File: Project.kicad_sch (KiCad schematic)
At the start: 21 parts, among them P1 USB_C_Plug, SW1 DOUBLE_KEY, U1 MAX15062A, U2 TUSB8041, Y1 24MHz

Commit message: 原理图完工
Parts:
- added C10, C11, C12, C13, C8, C9: 0.1uF, symbol Lib1:C(MM)-LibCool
- added C? (x2): 18pF, symbol Lib1:C(MM)-LibCool
- added C?: 4.7uF, symbol Lib1:C(MM)-LibCool
- added D1: OVERCUR1, symbol Device:LED
- added D2, D3: OVERCUR2, symbol Device:LED
- added J1, J2: USB3_A, symbol Connector:USB3_A
- added J?: RJ45, symbol Connector:RJ45
- added P2: USB_C_Plug, symbol Connector:USB_C_Plug
- added R10, R11: RES(M)-LibCool, symbol Lib1:RES(M)-LibCool
- added R9: 4.7K/5%, symbol Lib1:RES(M)-LibCool
- added R?: 226R/1%, symbol Lib1:RES(M)-LibCool
- added U?: XR22800, symbol Lib1:XR22800
- added Y?: 25MHz, symbol Lib1:OSC-LibCool
- gave numbers to parts that had none: 4
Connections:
- net +3V3: now also U2.16 (VDD33), U2.26 (USB_SSTXP_DN4), U2.34 (VDD33), U2.52 (VDD33), U2.63 (VDD33), C13.1, R10.1, R11.1, R9.1, U?.1 (VBUS_SENSE)
- net GND: now also U2.65 (VSS), C?.2, C?.2, C?.2, D1.1 (K), D2.1 (K), D3.1 (K), R?.2, U?.12 (GND), U?.21 (GND), U?.22 (GND), U?.28 (GND), U?.4 (GND)
- net POWER: now also J1.1 (VBUS), U?.7 (VCC)
- net at U2.1 (USB_DP_DN1): now also J1.3 (D+)
- net ETH_D-: now reaches U2.10 (USB_DM_DN2)
- net ETH_D-: now also U?.5 (USBD-)
- net at U2.17 (USB_DP_DN3): now also J2.3 (D+)
- net at U2.18 (USB_DM_DN3): now also J2.2 (D-)
- net at U2.19 (USB_SSTXP_DN3): now also C8.1
- net at U2.2 (USB_DM_DN1): now also J1.2 (D-)
- net at U2.20 (USB_SSTXM_DN3): now also C10.1
- net at U2.22 (USB_SSRXP_DN3): now also J2.6 (SSRX+)
- net at U2.23 (USB_SSRXM_DN3): now also J2.5 (SSRX-)
- net at U2.24 (USB_DP_DN4): now also P2.A6 (D+)
- net at U2.25 (USB_DM_DN4): now also P2.A7 (D-)
- net at U2.27 (USB_SSTXM_DN4): now also C12.1
- net at U2.29 (USB_SSRXP_DN4): now also P2.B11 (RX1+)
- net at U2.3 (USB_SSTXP_DN1): now also C9.1
- net at U2.30 (USB_SSRXM_DN4): now also P2.B10 (RX1-)
- net at U2.32 (PWRCTL4/BATEN4): now also R11.2
- net at U2.33 (PWRCTL3/BATEN3): now also R10.2
- net at U2.36 (PWRCTL1/BATEN1): now also R9.2
- net at U2.4 (USB_SSTXM_DN1): now also C11.1
- net at U2.43 (OVERCUR4z): now also D3.2 (A)
- net at U2.44 (OVERCUR3z): now also D2.2 (A)
- net at U2.46 (OVERCUR1z): now also D1.2 (A)
- net at U2.6 (USB_SSRXP_DN1): now also J1.6 (SSRX+)
- net at U2.7 (USB_SSRXM_DN1): now also J1.5 (SSRX-)
- net ETH_D+: now reaches U2.9 (USB_DP_DN2)
- net ETH_D+: now also U?.6 (USBD+)
- new net: C13.2, P2.A2 (TX1+)
- new net: C11.2, J1.8 (SSTX-)
- new net: C9.2, J1.9 (SSTX+)
- new net: C?.1, U?.10 (XTALIN), Y?.1
- new net: C?.1, U?.11 (3V3_OUT), U?.20 (CAP2), U?.3 (CAP1)
- new net: J?.2, U?.13 (ETH_TX-)
- new net: J?.1, U?.14 (ETH_TX+)
- new net: J?.3, U?.15 (ETH_RX+)
- new net: J?.6, U?.16 (ETH_RX-)
- new net: R?.1, U?.2 (REXT)
- new net: C?.1, U?.9 (XTALOUT), Y?.2
- new net: C12.2, P2.A3 (TX1-)
- new net: C10.2, J2.8 (SSTX-)
- new net: C8.2, J2.9 (SSTX+)
- new net: P2.A1 (GND), P2.A12 (GND), P2.B1 (GND), P2.B12 (GND)
- new net: P2.A4 (VBUS), P2.A9 (VBUS), P2.B4 (VBUS), P2.B9 (VBUS)
- no-connect marks 0 -> 22

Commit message: 画错了.png
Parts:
- R10, R11: value RES(M)-LibCool -> 4.7K/5%
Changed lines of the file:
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@@
       (effects (font (size 0.9906 0.9906)) (justify right))
     )
-    (property "Value" "RES(M)-LibCool" (id 1) (at 188.087 98.7288 90)
+    (property "Value" "4.7K/5%" (id 1) (at 188.087 98.7288 90)
       (effects (font (size 0.9906 0.9906)) (justify right))
     )
@@
       (effects (font (size 0.9906 0.9906)) (justify right))
     )
-    (property "Value" "RES(M)-LibCool" (id 1) (at 188.087 121.5888 90)
+    (property "Value" "4.7K/5%" (id 1) (at 188.087 121.5888 90)
       (effects (font (size 0.9906 0.9906)) (justify right))
     )
@@
     )
     (path "/89fb6906-a42e-497c-a7b2-25a3431a4030"
-      (reference "R10") (unit 1) (value "RES(M)-LibCool") (footprint "")
+      (reference "R10") (unit 1) (value "4.7K/5%") (footprint "")
     )
     (path "/df5779d8-f968-49f0-8166-ee0ca7a408f9"
-      (reference "R11") (unit 1) (value "RES(M)-LibCool") (footprint "")
+      (reference "R11") (unit 1) (value "4.7K/5%") (footprint "")
     )
     (path "/cb8a80c4-ebc1-408e-9240-fd24926bdfee"

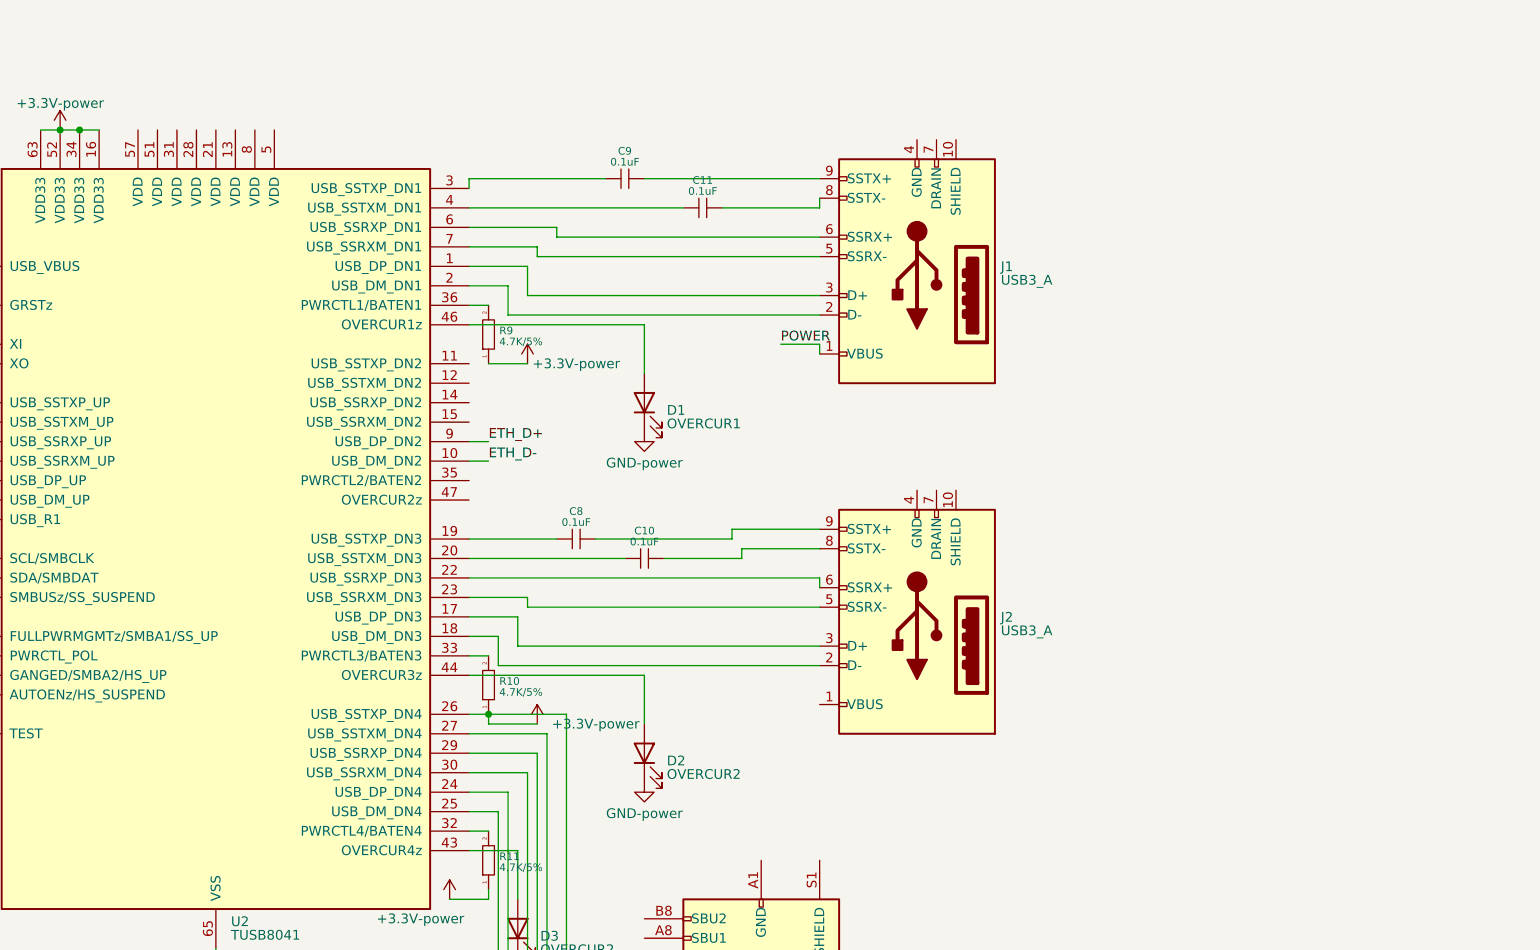
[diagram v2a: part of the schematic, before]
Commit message: 添加1.1v降压部分
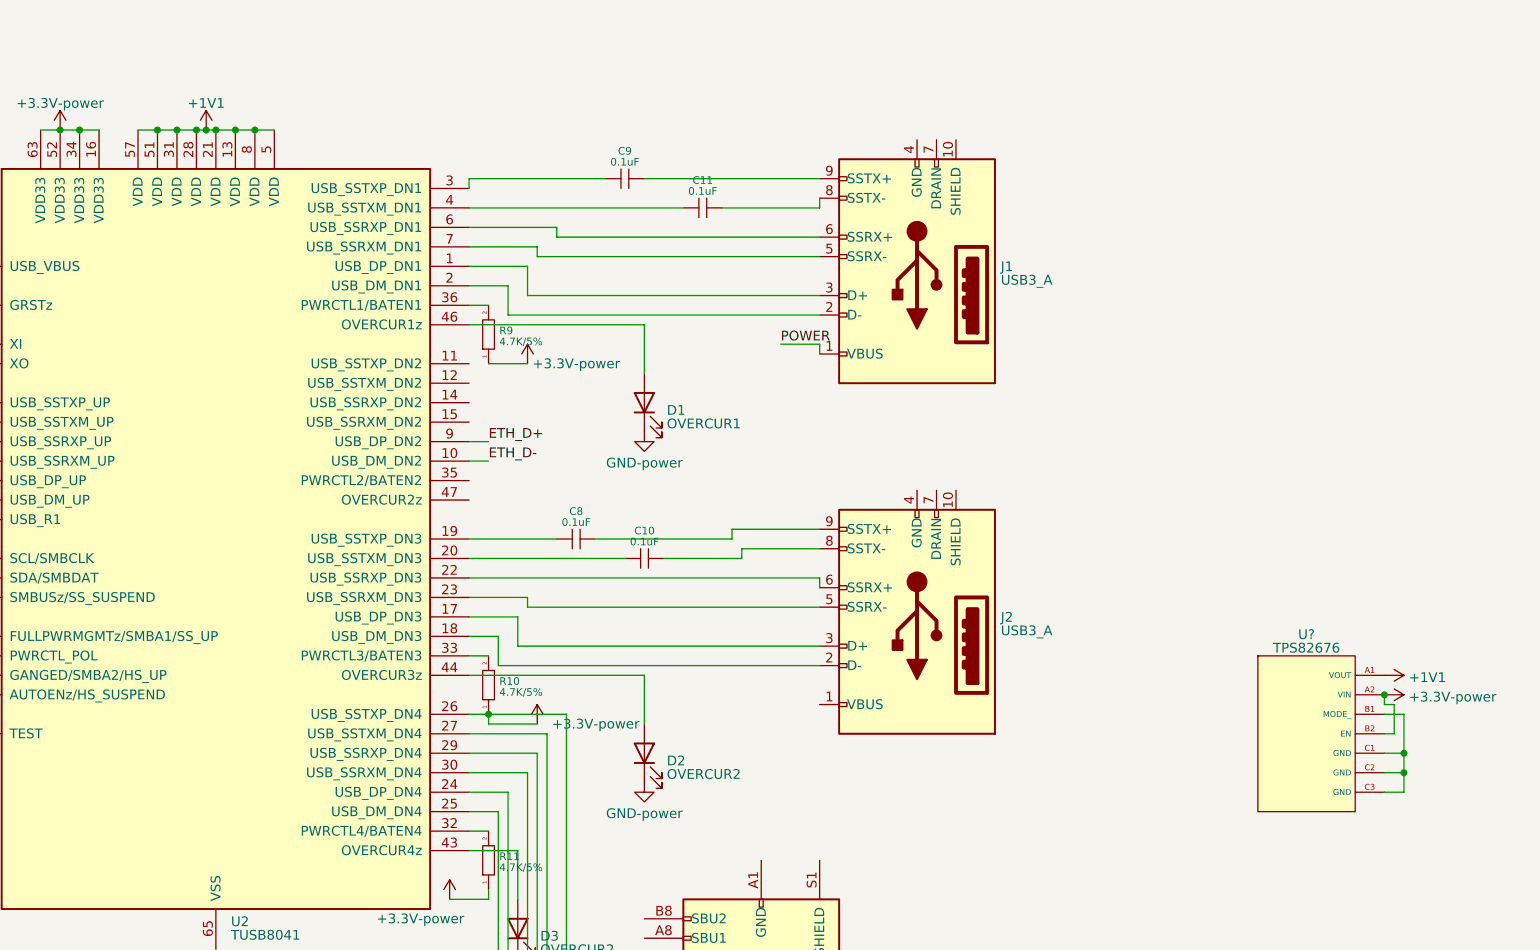
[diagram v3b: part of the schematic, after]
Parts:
- added U?: TPS82676, symbol Lib1:TPS82676
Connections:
- net +3V3: now also U?.A2 (VIN), U?.B2 (EN)
- net +1V1: now reaches U2.13 (VDD)
- net +1V1: now also U2.21 (VDD), U2.28 (VDD), U2.31 (VDD), U2.5 (VDD), U2.51 (VDD), U2.57 (VDD), U2.8 (VDD), U?.A1 (VOUT)
- new net: U?.B1 (MODE_), U?.C1 (GND), U?.C2 (GND), U?.C3 (GND)
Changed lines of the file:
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@@
   (junction (at 64.77 176.53) (diameter 0) (color 0 0 0 0)
   )
+  (junction (at 146.05 25.4) (diameter 0) (color 0 0 0 0)
+  )
   (junction (at 49.53 204.47) (diameter 0) (color 0 0 0 0)
   )
+  (junction (at 303.53 99.06) (diameter 0) (color 0 0 0 0)
+  )
   (junction (at 48.26 204.47) (diameter 0) (color 0 0 0 0)
   )
@@
   (junction (at 60.96 177.8) (diameter 0) (color 0 0 0 0)
   )
+  (junction (at 306.07 109.22) (diameter 0) (color 0 0 0 0)
+  )
   (junction (at 133.35 25.4) (diameter 0) (color 0 0 0 0)
   )
   (junction (at 58.42 194.31) (diameter 0) (color 0 0 0 0)
   )
+  (junction (at 143.51 25.4) (diameter 0) (color 0 0 0 0)
+  )
   (junction (at 69.85 177.8) (diameter 0) (color 0 0 0 0)
   )
+  (junction (at 149.86 25.4) (diameter 0) (color 0 0 0 0)
+  )
   (junction (at 101.6 54.61) (diameter 0) (color 0 0 0 0)
   )
   (junction (at 110.49 43.18) (diameter 0) (color 0 0 0 0)
   )
+  (junction (at 153.67 25.4) (diameter 0) (color 0 0 0 0)
+  )
   (junction (at 130.81 25.4) (diameter 0) (color 0 0 0 0)
   )
@@
   (junction (at 24.13 86.36) (diameter 0) (color 0 0 0 0)
   )
+  (junction (at 156.21 25.4) (diameter 0) (color 0 0 0 0)
+  )
   (junction (at 114.3 50.8) (diameter 0) (color 0 0 0 0)
   )
+  (junction (at 306.07 106.68) (diameter 0) (color 0 0 0 0)
+  )
   (junction (at 106.68 58.42) (diameter 0) (color 0 0 0 0)
   )
@@
   )
   (junction (at 114.3 58.42) (diameter 0) (color 0 0 0 0)
+  )
+  (junction (at 151.13 25.4) (diameter 0) (color 0 0 0 0)
+  )
+  (junction (at 148.59 25.4) (diameter 0) (color 0 0 0 0)
   )
   (no_connect (at 39.37 186.69))
@@
   (no_connect (at 43.18 78.74))
   (no_connect (at 57.15 193.04))
+  (wire (pts (xy 306.07 101.6) (xy 306.07 106.68))
+    (stroke (width 0) (type default))
+  )
+  (wire (pts (xy 143.51 25.4) (xy 146.05 25.4))
+    (stroke (width 0) (type default))
+  )
   (wire (pts (xy 110.49 43.18) (xy 118.11 43.18))
     (stroke (width 0) (type default))
@@
     (stroke (width 0) (type default))
   )
+  (wire (pts (xy 151.13 25.4) (xy 153.67 25.4))
+    (stroke (width 0) (type default))
+  )
   (wire (pts (xy 184.15 50.8) (xy 207.01 50.8))
     (stroke (width 0) (type default))
@@
     (stroke (width 0) (type default))
   )
+  (wire (pts (xy 303.53 109.22) (xy 306.07 109.22))
+    (stroke (width 0) (type default))
+  )
   (wire (pts (xy 193.04 106.68) (xy 193.04 158.75))
     (stroke (width 0) (type default))
@@
     (stroke (width 0) (type default))
   )
+  (wire (pts (xy 153.67 25.4) (xy 156.21 25.4))
+    (stroke (width 0) (type default))
+  )
   (wire (pts (xy 229.87 46.99) (xy 191.77 46.99))
     (stroke (width 0) (type default))
   )
+  (wire (pts (xy 306.07 109.22) (xy 306.07 106.68))
+    (stroke (width 0) (type default))
+  )
   (wire (pts (xy 114.3 63.5) (xy 118.11 63.5))
     (stroke (width 0) (type default))
@@
     (stroke (width 0) (type default))
   )
+  (wire (pts (xy 306.07 109.22) (xy 306.07 111.76))
+    (stroke (width 0) (type default))
+  )
   (wire (pts (xy 189.23 49.53) (xy 229.87 49.53))
     (stroke (width 0) (type default))
@@
     (stroke (width 0) (type default))
   )
+  (wire (pts (xy 156.21 25.4) (xy 158.75 25.4))
+    (stroke (width 0) (type default))
+  )
   (wire (pts (xy 34.29 121.92) (xy 35.56 121.92))
     (stroke (width 0) (type default))
@@
     (stroke (width 0) (type default))
   )
+  (wire (pts (xy 306.07 111.76) (xy 303.53 111.76))
+    (stroke (width 0) (type default))
+  )
   (wire (pts (xy 191.77 161.29) (xy 207.01 161.29))
     (stroke (width 0) (type default))
@@
     (stroke (width 0) (type default))
   )
+  (wire (pts (xy 148.59 25.4) (xy 149.86 25.4))
+    (stroke (width 0) (type default))
+  )
   (wire (pts (xy 207.01 96.52) (xy 207.01 102.87))
     (stroke (width 0) (type default))
@@
     (stroke (width 0) (type default))
   )
+  (wire (pts (xy 304.8 100.33) (xy 304.8 104.14))
+    (stroke (width 0) (type default))
+  )
   (wire (pts (xy 200.66 78.74) (xy 218.44 78.74))
     (stroke (width 0) (type default))
@@
     (stroke (width 0) (type default))
   )
+  (wire (pts (xy 303.53 99.06) (xy 303.53 100.33))
+    (stroke (width 0) (type default))
+  )
   (wire (pts (xy 184.15 78.74) (xy 195.58 78.74))
     (stroke (width 0) (type default))
   )
+  (wire (pts (xy 146.05 25.4) (xy 148.59 25.4))
+    (stroke (width 0) (type default))
+  )
   (wire (pts (xy 229.87 39.37) (xy 195.58 39.37))
     (stroke (width 0) (type default))
   )
+  (wire (pts (xy 149.86 25.4) (xy 151.13 25.4))
+    (stroke (width 0) (type default))
+  )
   (wire (pts (xy 106.68 50.8) (xy 114.3 50.8))
     (stroke (width 0) (type default))
@@
     (stroke (width 0) (type default))
   )
+  (wire (pts (xy 306.07 106.68) (xy 303.53 106.68))
+    (stroke (width 0) (type default))
+  )
   (wire (pts (xy 72.39 184.15) (xy 72.39 186.69))
     (stroke (width 0) (type default))
@@
     (stroke (width 0) (type default))
   )
+  (wire (pts (xy 303.53 100.33) (xy 304.8 100.33))
+    (stroke (width 0) (type default))
+  )
   (wire (pts (xy 229.87 35.56) (xy 229.87 34.29))
     (stroke (width 0) (type default))
@@
     (stroke (width 0) (type default))
   )
+  (wire (pts (xy 303.53 101.6) (xy 306.07 101.6))
+    (stroke (width 0) (type default))
+  )
   (wire (pts (xy 43.18 38.1) (xy 46.99 38.1))
     (stroke (width 0) (type default))
@@
     (stroke (width 0) (type default))
   )
+  (wire (pts (xy 304.8 104.14) (xy 303.53 104.14))
+    (stroke (width 0) (type default))
+  )
   (wire (pts (xy 184.15 106.68) (xy 193.04 106.68))
     (stroke (width 0) (type default))
@@
   )
   (wire (pts (xy 191.77 46.99) (xy 191.77 43.18))
+    (stroke (width 0) (type default))
+  )
+  (wire (pts (xy 140.97 25.4) (xy 143.51 25.4))
     (stroke (width 0) (type default))
   )
@@
     (pin "1")
     (pin "2")
+  )
+  (symbol (lib_id "power:+1V1") (at 303.53 96.52 270) (unit 1)
+    (in_bom yes) (on_board yes) (fields_autoplaced)
+    (property "Reference" "#PWR?" (id 0) (at 299.72 96.52 0)
+      (effects (font (size 1.27 1.27)) hide)
+    )
+    (property "Value" "+1V1" (id 1) (at 306.705 96.8066 90)
+      (effects (font (size 1.27 1.27)) (justify left))
+    )
+    (property "Footprint" "" (id 2) (at 303.53 96.52 0)
+      (effects (font (size 1.27 1.27)) hide)
+    )
+    (property "Datasheet" "" (id 3) (at 303.53 96.52 0)
+      (effects (font (size 1.27 1.27)) hide)
+    )
+    (pin "1")
   )
   (symbol (lib_id "Interface_USB:TUSB8041") (at 151.13 78.74 0) (unit 1)
@@
     (pin "2")
   )
+  (symbol (lib_id "Lib1:TPS82676") (at 293.37 92.71 0) (unit 1)
+    (in_bom yes) (on_board yes) (fields_autoplaced)
+    (property "Reference" "U?" (id 0) (at 293.37 91.1987 0)
+      (effects (font (size 1.27 1.27)))
+    )
+    (property "Value" "TPS82676" (id 1) (at 293.37 92.9609 0)
+      (effects (font (size 1.27 1.27)))
+    )
+    (property "Footprint" "" (id 2) (at 293.37 92.71 0)
+      (effects (font (size 1.27 1.27)) hide)
+    )
+    (property "Datasheet" "" (id 3) (at 293.37 92.71 0)
+      (effects (font (size 1.27 1.27)) hide)
+    )
+    (pin "A1")
+    (pin "A2")
+    (pin "B1")
+    (pin "B2")
+    (pin "C1")
+    (pin "C2")
+    (pin "C3")
+  )
   (symbol (lib_id "Lib1:C(MM)-LibCool") (at 44.45 17.78 90) (unit 1)
     (in_bom yes) (on_board yes) (fields_autoplaced)
@@
     )
     (property "Datasheet" "" (id 3) (at 191.77 55.88 0)
+      (effects (font (size 1.27 1.27)) hide)
+    )
+    (pin "1")
+  )
+  (symbol (lib_id "Lib1:+3.3V-power") (at 303.53 99.06 270) (unit 1)
+    (in_bom yes) (on_board yes) (fields_autoplaced)
+    (property "Reference" "#PWR?" (id 0) (at 299.72 99.06 0)
+      (effects (font (size 1.27 1.27)) hide)
+    )
+    (property "Value" "+3.3V-power" (id 1) (at 306.705 99.3466 90)
+      (effects (font (size 1.27 1.27)) (justify left))
+    )
+    (property "Footprint" "" (id 2) (at 303.53 99.06 0)
+      (effects (font (size 1.27 1.27)) hide)
+    )
+    (property "Datasheet" "" (id 3) (at 303.53 99.06 0)
       (effects (font (size 1.27 1.27)) hide)
     )
@@
     (pin "S1")
   )
+  (symbol (lib_id "power:+1V1") (at 149.86 25.4 0) (unit 1)
+    (in_bom yes) (on_board yes) (fields_autoplaced)
+    (property "Reference" "#PWR?" (id 0) (at 149.86 29.21 0)
+      (effects (font (size 1.27 1.27)) hide)
+    )
+    (property "Value" "+1V1" (id 1) (at 149.86 21.9171 0)
+      (effects (font (size 1.27 1.27)))
+    )
+    (property "Footprint" "" (id 2) (at 149.86 25.4 0)
+      (effects (font (size 1.27 1.27)) hide)
+    )
+    (property "Datasheet" "" (id 3) (at 149.86 25.4 0)
+      (effects (font (size 1.27 1.27)) hide)
+    )
+    (pin "1")
+  )
   (symbol (lib_id "Lib1:+3.3V-power") (at 57.15 175.26 0) (unit 1)
     (in_bom yes) (on_board yes) (fields_autoplaced)
@@
       (reference "#PWR?") (unit 1) (value "GND-power") (footprint "")
     )
+    (path "/69bb625f-a2cc-49f3-a551-f3c5c377daba"
+      (reference "#PWR?") (unit 1) (value "+1V1") (footprint "")
+    )
+    (path "/c3584b5b-dee2-402a-b919-18dc23406c53"
+      (reference "#PWR?") (unit 1) (value "+3.3V-power") (footprint "")
+    )
     (path "/de5c5318-1db2-43b6-8702-ed17e692413f"
       (reference "#PWR?") (unit 1) (value "GND-power") (footprint "")
     )
+    (path "/e32d2ccd-1996-4d9f-a537-20b2b5a962c5"
+      (reference "#PWR?") (unit 1) (value "+1V1") (footprint "")
+    )
     (path "/e458f3a0-7211-43d9-af4d-2610967466d6"
       (reference "#PWR?") (unit 1) (value "+3.3V-power") (footprint "")
@@
       (reference "U?") (unit 1) (value "XR22800") (footprint "")
     )
+    (path "/a3ac1d4f-eda0-4055-beb0-f7012038f34c"
+      (reference "U?") (unit 1) (value "TPS82676") (footprint "")
+    )
     (path "/142d58ca-db89-4877-926e-13ac5ef0d795"
